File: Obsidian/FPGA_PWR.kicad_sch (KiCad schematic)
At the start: 52 parts, among them U1 XC7A35T-CSG325

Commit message: update with available components on LCSC
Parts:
- C100, C101, C102, C112, C121, C97, C98, C99: LCSC (none) -> C565524
- C103, C104, C105, C106, C107, C108, C117, C118, C156, C161, C162, C167, C168: LCSC (none) -> C318563
- C109, C110, C111, C119, C122: LCSC (none) -> C141660
- C113, C114, C115, C116, C120, C155, C89, C90, C91, C92, C93, C94, C95, C96: LCSC (none) -> C85926
- C157, C158, C159, C160, C163, C164, C165, C166, C169: LCSC (none) -> C190187
- L16: LCSC (none) -> C88966
- R114: LCSC (none) -> C413063
- U1: FT Rotation Offset (none) -> 0; LCSC (none) -> C1521749

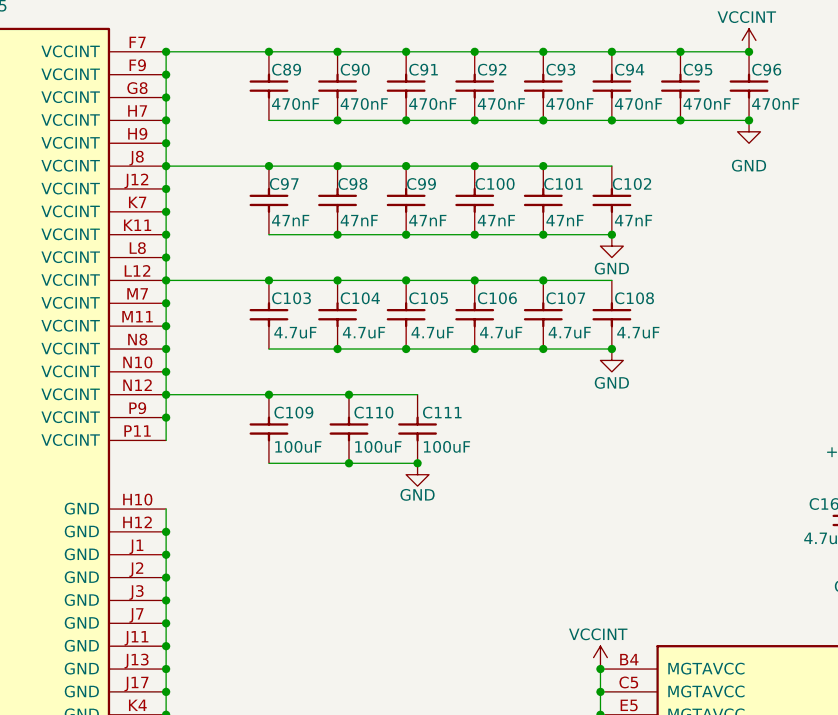
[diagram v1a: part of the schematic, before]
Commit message: Adding symbol library
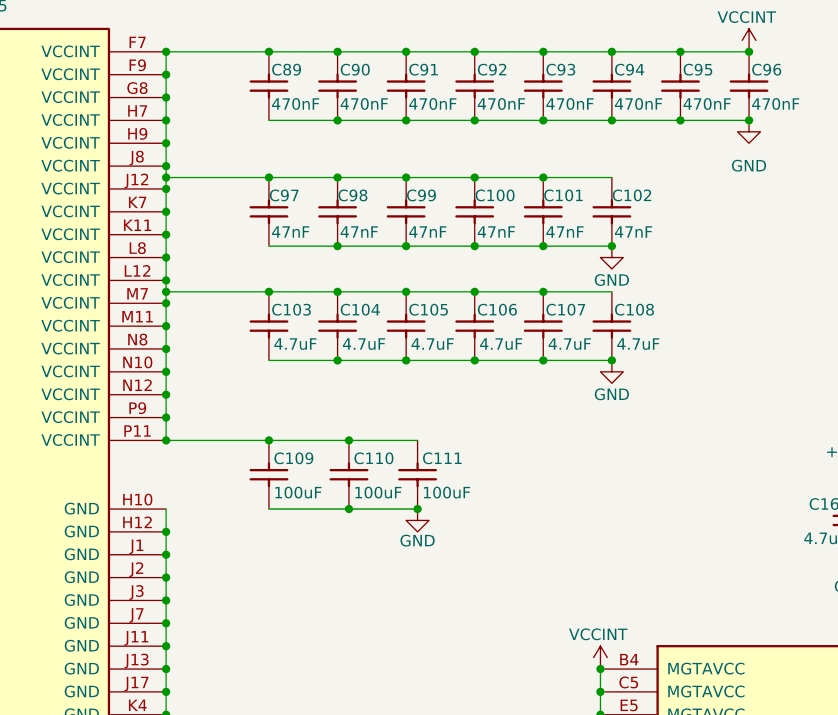
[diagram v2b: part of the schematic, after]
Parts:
- C100, C101, C102, C112, C121, C97, C98, C99: symbol Capacitors SMD:CC0201_47NF_6.3V_10%_X5R -> Library_Symbol:CC0201_47NF_6.3V_10%_X5R
- C103, C104, C105, C106, C107, C108, C117, C118, C156, C161, C162, C167, C168: symbol Capacitors SMD:CC0402_4.7UF_16V_20%_X5R -> Library_Symbol:CC0402_4.7UF_16V_20%_X5R
- C109, C110, C111, C119, C122: symbol Capacitors SMD:CC0805_100UF_6.3V_20%_X5R -> Library_Symbol:CC0805_100UF_6.3V_20%_X5R
- C113, C114, C115, C116, C120, C155, C89, C90, C91, C92, C93, C94, C95, C96: symbol Capacitors SMD:CC0201_470NF_4V_20%_X5R -> Library_Symbol:CC0201_470NF_4V_20%_X5R
- C157, C158, C159, C160, C163, C164, C165, C166, C169: symbol Capacitors SMD:CC0201_100NF_6.3V_10%_X5R -> Library_Symbol:CC0201_100NF_6.3V_10%_X5R
- L16: symbol Inductors SMD:IND0402_MURATA_BLM15HB221SN1 -> Library_Symbol:IND0402_MURATA_BLM15HB221SN1
- R114: symbol Resistors_SMD:R0402_100R_1%_0.1W_100PPM -> Library_Symbol:R0402_100R_1%_0.1W_100PPM
- U1: symbol FPGA_Xilinx_Artix7:XC7A35T-CSG325 -> Library_Symbol:XC7A35T-CSG325
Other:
- moved on the sheet: C100, C101, C102, C103, C104, C105, C106, C107, C108, C109, C110, C111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

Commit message: Correct Schematic errors
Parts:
- C100, C101, C102, C112, C113, C114, C115, C116, C120, C121, C155, C157, C158, C159, C160, C163, C164, C165, C166, C169, C89, C90, C91, C92, C93, C94, C95, C96, C97, C98, C99: footprint Capacitors SMD:CAPC0603X33N -> Footprint:CAPC0603X33N
- C103, C104, C105, C106, C107, C108, C117, C118, C156, C161, C162, C167, C168: footprint Capacitors SMD:CAPC1005X55N -> Footprint:CAPC1005X55N
- C109, C110, C111, C119, C122: footprint Capacitors SMD:CAPC2012X145N -> Footprint:CAPC2012X145N
- L16: footprint Inductors SMD:INDC1005X55N -> Footprint:INDC1005X55N
- R114: footprint RESC1005X40N -> Footprint:RESC1005X40N; Database Table Name (none) -> Resistors; Footprint Library (none) -> Resistors SMD; HelpURL (none) -> \\cern.ch\dfs\Applications\Altium\Datasheets\R0402_Phycomp_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
- U1: footprint Package_BGA:Xilinx_CSG325 -> Footprint:Xilinx_CSG325
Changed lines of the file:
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@@
 			)
 		)
-		(property "Footprint" "Capacitors SMD:CAPC1005X55N"
+		(property "Footprint" "Footprint:CAPC1005X55N"
 			(at 154.178 66.04 0)
 			(effects
@@
 			)
 		)
-		(property "Footprint" "Capacitors SMD:CAPC1005X55N"
+		(property "Footprint" "Footprint:CAPC1005X55N"
 			(at 146.558 66.04 0)
 			(effects
@@
 			)
 		)
-		(property "Footprint" "Capacitors SMD:CAPC2012X145N"
+		(property "Footprint" "Footprint:CAPC2012X145N"
 			(at 163.068 82.55 0)
 			(effects
@@
 			)
 		)
-		(property "Footprint" "Package_BGA:Xilinx_CSG325"
+		(property "Footprint" "Footprint:Xilinx_CSG325"
 			(at 213.36 107.95 0)
 			(effects
@@
 			)
 		)
-		(property "Footprint" "Capacitors SMD:CAPC0603X33N"
+		(property "Footprint" "Footprint:CAPC0603X33N"
 			(at 199.898 39.37 0)
 			(effects
@@
 			)
 		)
-		(property "Footprint" "Capacitors SMD:CAPC0603X33N"
+		(property "Footprint" "Footprint:CAPC0603X33N"
 			(at 154.178 39.37 0)
 			(effects
@@
 			)
 		)
-		(property "Footprint" "Capacitors SMD:CAPC1005X55N"
+		(property "Footprint" "Footprint:CAPC1005X55N"
 			(at 218.948 132.08 0)
 			(effects
@@
 			)
 		)
-		(property "Footprint" "Capacitors SMD:CAPC0603X33N"
+		(property "Footprint" "Footprint:CAPC0603X33N"
 			(at 161.798 53.34 0)
 			(effects
@@
 			)
 		)
-		(property "Footprint" "Capacitors SMD:CAPC0603X33N"
+		(property "Footprint" "Footprint:CAPC0603X33N"
 			(at 169.418 53.34 0)
 			(effects
@@
 			)
 		)
-		(property "Footprint" "Capacitors SMD:CAPC0603X33N"
+		(property "Footprint" "Footprint:CAPC0603X33N"
 			(at 198.628 132.08 0)
 			(effects
@@
 			)
 		)
-		(property "Footprint" "Capacitors SMD:CAPC0603X33N"
+		(property "Footprint" "Footprint:CAPC0603X33N"
 			(at 177.038 53.34 0)
 			(effects
@@
 			)
 		)
-		(property "Footprint" "Capacitors SMD:CAPC0603X33N"
+		(property "Footprint" "Footprint:CAPC0603X33N"
 			(at 184.658 39.37 0)
 			(effects
@@
 			)
 		)
-		(property "Footprint" "Capacitors SMD:CAPC0603X33N"
+		(property "Footprint" "Footprint:CAPC0603X33N"
 			(at 231.648 87.63 0)
 			(effects
@@
 			)
 		)
-		(property "Footprint" "Capacitors SMD:CAPC1005X55N"
+		(property "Footprint" "Footprint:CAPC1005X55N"
 			(at 177.038 66.04 0)
 			(effects
@@
 			)
 		)
-		(property "Footprint" "Capacitors SMD:CAPC0603X33N"
+		(property "Footprint" "Footprint:CAPC0603X33N"
 			(at 169.418 39.37 0)
 			(effects
@@
 			)
 		)
-		(property "Footprint" "Capacitors SMD:CAPC0603X33N"
+		(property "Footprint" "Footprint:CAPC0603X33N"
 			(at 70.358 33.02 0)
 			(effects
@@
 			)
 		)
-		(property "Footprint" "Capacitors SMD:CAPC0603X33N"
+		(property "Footprint" "Footprint:CAPC0603X33N"
 			(at 146.558 53.34 0)
 			(effects
@@
 			)
 		)
-		(property "Footprint" "Capacitors SMD:CAPC2012X145N"
+		(property "Footprint" "Footprint:CAPC2012X145N"
 			(at 146.558 82.55 0)
 			(effects
@@
 			)
 		)
-		(property "Footprint" "Capacitors SMD:CAPC0603X33N"
+		(property "Footprint" "Footprint:CAPC0603X33N"
 			(at 65.278 74.93 0)
 			(effects
@@
 			)
 		)
-		(property "Footprint" "Capacitors SMD:CAPC0603X33N"
+		(property "Footprint" "Footprint:CAPC0603X33N"
 			(at 224.028 87.63 0)
 			(effects
@@
 			)
 		)
-		(property "Footprint" "Capacitors SMD:CAPC0603X33N"
+		(property "Footprint" "Footprint:CAPC0603X33N"
 			(at 61.468 57.15 0)
 			(effects
@@
 			)
 		)
-		(property "Footprint" "Capacitors SMD:CAPC0603X33N"
+		(property "Footprint" "Footprint:CAPC0603X33N"
 			(at 79.248 33.02 0)
 			(effects
@@
 			)
 		)
-		(property "Footprint" "Capacitors SMD:CAPC2012X145N"
+		(property "Footprint" "Footprint:CAPC2012X145N"
 			(at 155.448 82.55 0)
 			(effects
@@
 			)
 		)
-		(property "Footprint" "Capacitors SMD:CAPC0603X33N"
+		(property "Footprint" "Footprint:CAPC0603X33N"
 			(at 254.508 87.63 0)
 			(effects
@@
 			)
 		)
-		(property "Footprint" "Capacitors SMD:CAPC2012X145N"
+		(property "Footprint" "Footprint:CAPC2012X145N"
 			(at 24.638 33.02 0)
 			(effects
@@
 			)
 		)
-		(property "Footprint" "Package_BGA:Xilinx_CSG325"
+		(property "Footprint" "Footprint:Xilinx_CSG325"
 			(at 101.6 102.87 0)
 			(effects
@@
 			)
 		)
-		(property "Footprint" "Capacitors SMD:CAPC0603X33N"
+		(property "Footprint" "Footprint:CAPC0603X33N"
 			(at 62.738 33.02 0)
 			(effects
@@
 			)
 		)
-		(property "Footprint" "RESC1005X40N"
+		(property "Footprint" "Footprint:RESC1005X40N"
 			(at 251.46 141.478 0)
 			(effects
@@
 			)
 		)
+		(property "Database Table Name" "Resistors"
+			(at 251.46 115.57 0)
+			(effects
+				(font
+					(size 1.27 1.27)
+				)
+				(hide yes)
+			)
+		)
+		(property "Footprint Library" "Resistors SMD"
+			(at 251.46 115.57 0)
+			(effects
+				(font
+					(size 1.27 1.27)
+				)
+				(hide yes)
+			)
+		)
+		(property "HelpURL" "\\\\cern.ch\\dfs\\Applications\\Altium\\Datasheets\\R0402_Phycomp_RC0402.pdf"
+			(at 251.46 115.57 0)
+			(effects
+				(font
+					(size 1.27 1.27)
+				)
+				(hide yes)
+			)
+		)
 		(pin "1"
 		)
@@
 			)
 		)
-		(property "Footprint" "Capacitors SMD:CAPC0603X33N"
+		(property "Footprint" "Footprint:CAPC0603X33N"
 			(at 177.038 39.37 0)
 			(effects
@@
 			)
 		)
-		(property "Footprint" "Capacitors SMD:CAPC0603X33N"
+		(property "Footprint" "Footprint:CAPC0603X33N"
 			(at 74.168 74.93 0)
 			(effects
@@
 			)
 		)
-		(property "Footprint" "Capacitors SMD:CAPC1005X55N"
+		(property "Footprint" "Footprint:CAPC1005X55N"
 			(at 33.528 33.02 0)
 			(effects
@@
 			)
 		)
-		(property "Footprint" "Capacitors SMD:CAPC2012X145N"
+		(property "Footprint" "Footprint:CAPC2012X145N"
 			(at 57.658 74.93 0)
 			(effects
@@
 			)
 		)
-		(property "Footprint" "Inductors SMD:INDC1005X55N"
+		(property "Footprint" "Footprint:INDC1005X55N"
 			(at 39.37 56.388 0)
 			(effects
@@
 			)
 		)
-		(property "Footprint" "Capacitors SMD:CAPC0603X33N"
+		(property "Footprint" "Footprint:CAPC0603X33N"
 			(at 183.388 132.08 0)
 			(effects
@@
 			)
 		)
-		(property "Footprint" "Capacitors SMD:CAPC0603X33N"
+		(property "Footprint" "Footprint:CAPC0603X33N"
 			(at 184.658 53.34 0)
 			(effects
@@
 			)
 		)
-		(property "Footprint" "Capacitors SMD:CAPC0603X33N"
+		(property "Footprint" "Footprint:CAPC0603X33N"
 			(at 55.118 33.02 0)
 			(effects
@@
 			)
 		)
-		(property "Footprint" "Capacitors SMD:CAPC1005X55N"
+		(property "Footprint" "Footprint:CAPC1005X55N"
 			(at 211.328 132.08 0)
 			(effects
@@
 			)
 		)
-		(property "Footprint" "Capacitors SMD:CAPC0603X33N"
+		(property "Footprint" "Footprint:CAPC0603X33N"
 			(at 192.278 39.37 0)
 			(effects
@@
 			)
 		)
-		(property "Footprint" "Capacitors SMD:CAPC0603X33N"
+		(property "Footprint" "Footprint:CAPC0603X33N"
 			(at 246.888 87.63 0)
 			(effects
@@
 			)
 		)
-		(property "Footprint" "Capacitors SMD:CAPC1005X55N"
+		(property "Footprint" "Footprint:CAPC1005X55N"
 			(at 169.418 66.04 0)
 			(effects
@@
 			)
 		)
-		(property "Footprint" "Capacitors SMD:CAPC1005X55N"
+		(property "Footprint" "Footprint:CAPC1005X55N"
 			(at 161.798 66.04 0)
 			(effects
@@
 			)
 		)
-		(property "Footprint" "Capacitors SMD:CAPC0603X33N"
+		(property "Footprint" "Footprint:CAPC0603X33N"
 			(at 191.008 132.08 0)
 			(effects
@@
 			)
 		)
-		(property "Footprint" "Capacitors SMD:CAPC0603X33N"
+		(property "Footprint" "Footprint:CAPC0603X33N"
 			(at 154.178 53.34 0)
 			(effects
@@
 			)
 		)
-		(property "Footprint" "Capacitors SMD:CAPC0603X33N"
+		(property "Footprint" "Footprint:CAPC0603X33N"
 			(at 146.558 39.37 0)
 			(effects
@@
 			)
 		)
-		(property "Footprint" "Capacitors SMD:CAPC1005X55N"
+		(property "Footprint" "Footprint:CAPC1005X55N"
 			(at 202.692 87.63 0)
 			(effects
@@
 			)
 		)
-		(property "Footprint" "Capacitors SMD:CAPC1005X55N"
+		(property "Footprint" "Footprint:CAPC1005X55N"
 			(at 195.072 87.63 0)
 			(effects
@@
 			)
 		)
-		(property "Footprint" "Capacitors SMD:CAPC0603X33N"
+		(property "Footprint" "Footprint:CAPC0603X33N"
 			(at 239.268 87.63 0)
 			(effects
@@
 			)
 		)
-		(property "Footprint" "Capacitors SMD:CAPC1005X55N"
+		(property "Footprint" "Footprint:CAPC1005X55N"
 			(at 38.608 57.15 0)
 			(effects
@@
 			)
 		)
-		(property "Footprint" "Capacitors SMD:CAPC1005X55N"
+		(property "Footprint" "Footprint:CAPC1005X55N"
 			(at 41.148 33.02 0)
 			(effects
@@
 			)
 		)
-		(property "Footprint" "Capacitors SMD:CAPC1005X55N"
+		(property "Footprint" "Footprint:CAPC1005X55N"
 			(at 184.658 66.04 0)
 			(effects
@@
 			)
 		)
-		(property "Footprint" "Capacitors SMD:CAPC0603X33N"
+		(property "Footprint" "Footprint:CAPC0603X33N"
 			(at 47.498 33.02 0)
 			(effects
@@
 			)
 		)
-		(property "Footprint" "Capacitors SMD:CAPC0603X33N"
+		(property "Footprint" "Footprint:CAPC0603X33N"
 			(at 204.978 132.08 0)
 			(effects
@@
 			)
 		)
-		(property "Footprint" "Capacitors SMD:CAPC0603X33N"
+		(property "Footprint" "Footprint:CAPC0603X33N"
 			(at 161.798 39.37 0)
 			(effects

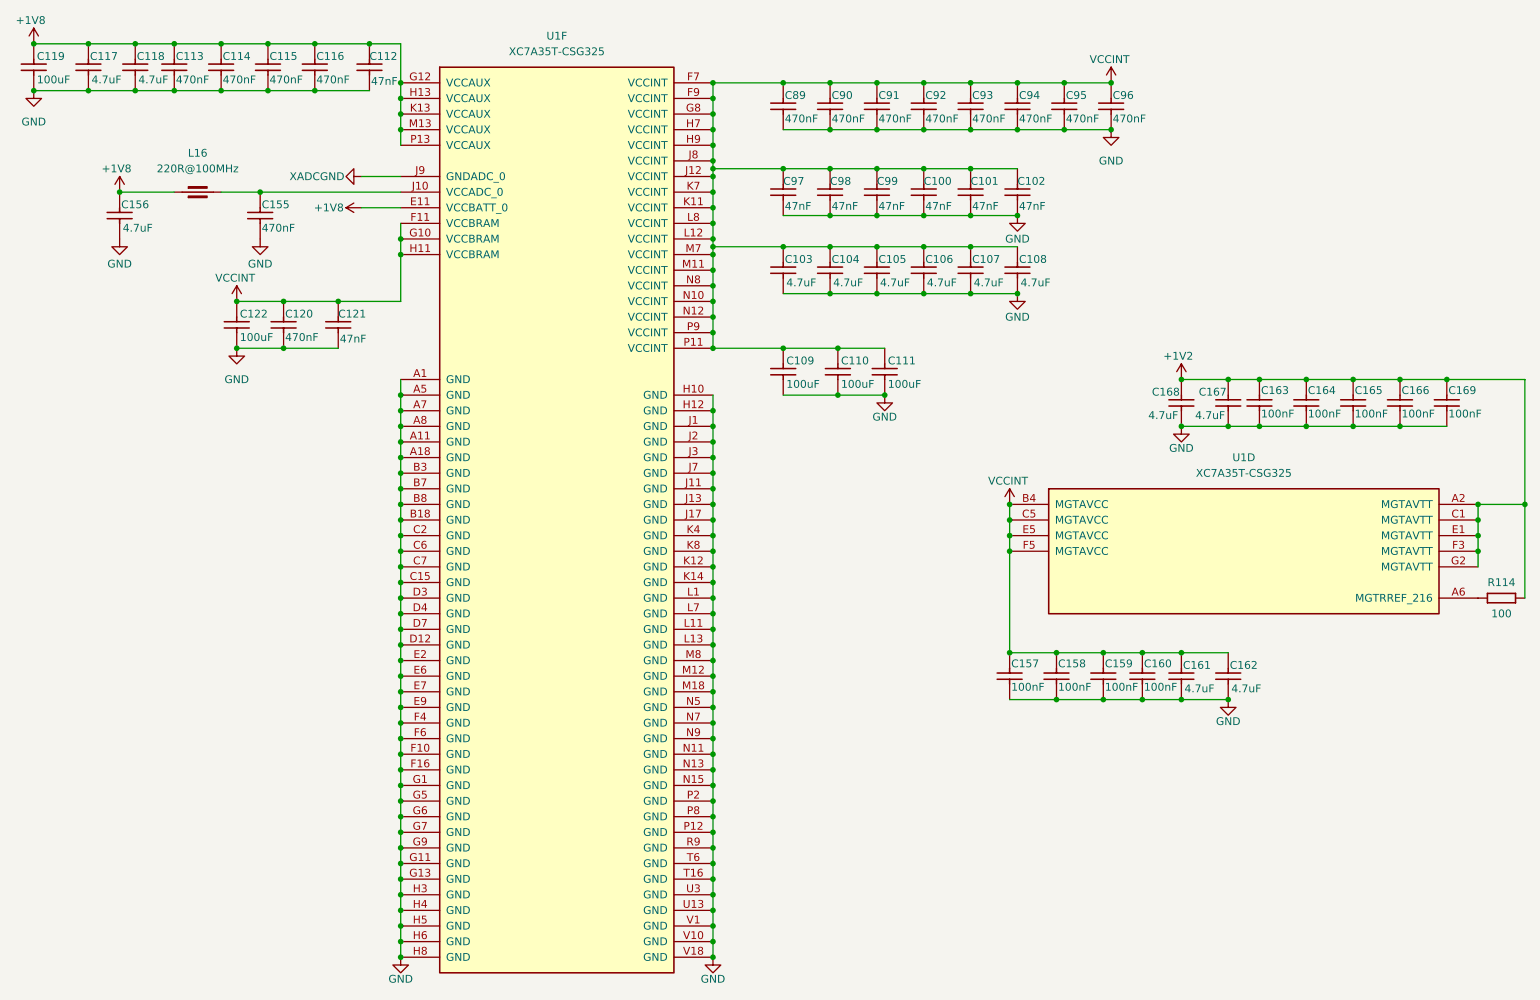
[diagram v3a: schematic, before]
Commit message: deleting two labels on 1V net, replacing with VCCINT_1V
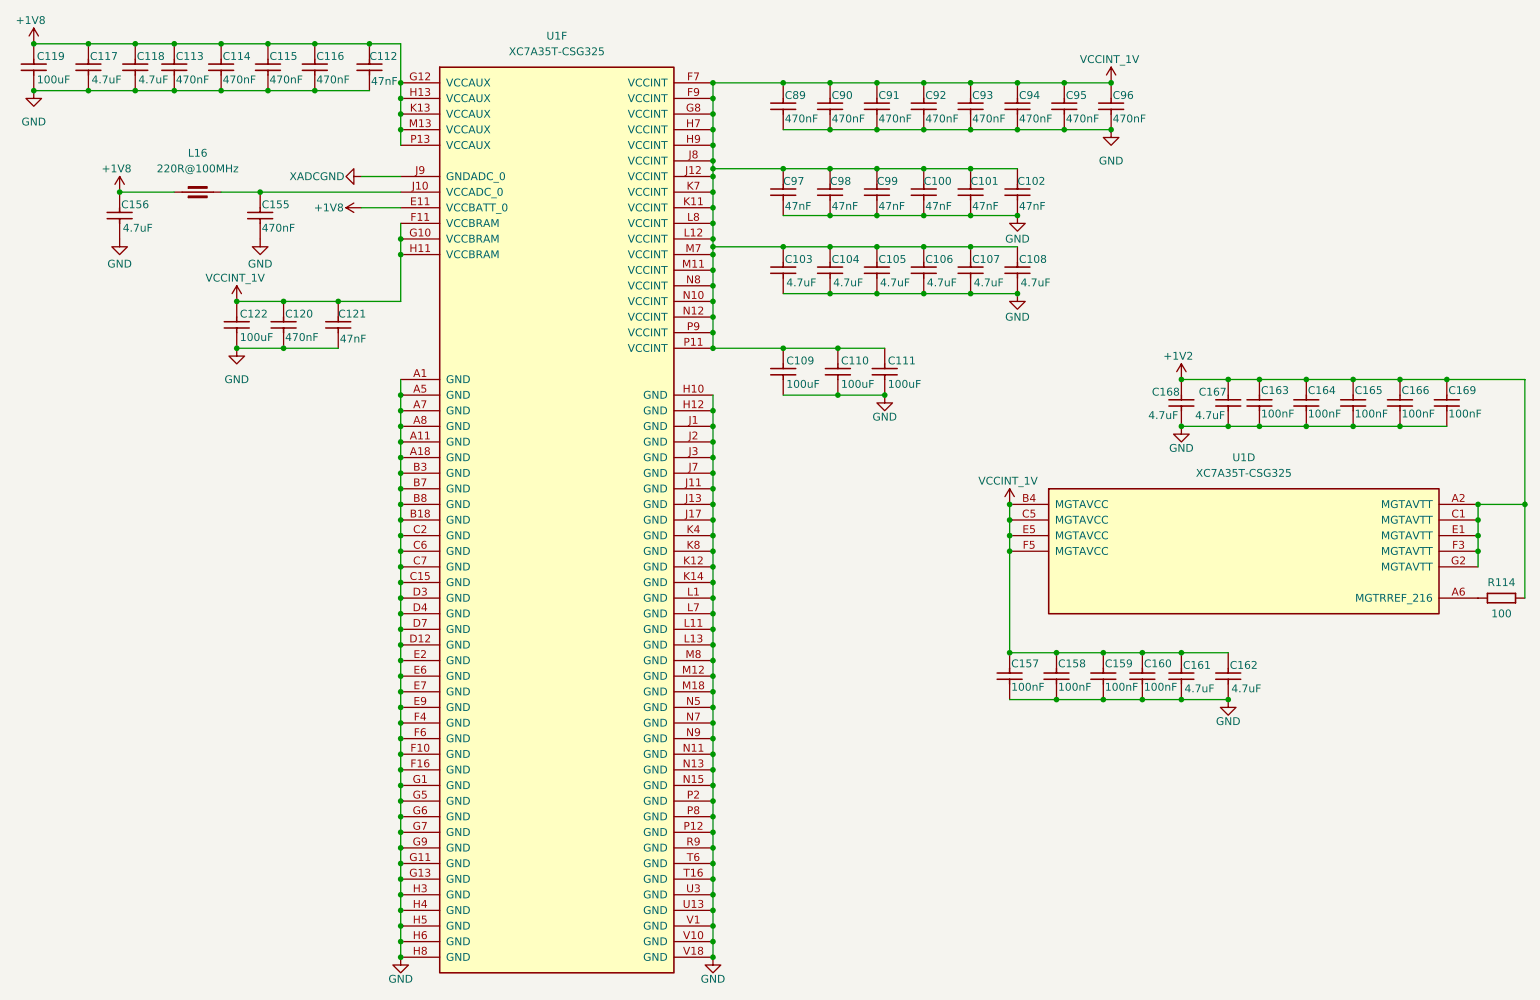
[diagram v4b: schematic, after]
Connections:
- net VCCINT renamed VCCINT_1V
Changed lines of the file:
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@@
 			)
 		)
-		(property "Value" "VCCINT"
+		(property "Value" "VCCINT_1V"
 			(at 175.006 96.52 0)
 			(effects
@@
 			)
 		)
-		(property "Value" "VCCINT"
+		(property "Value" "VCCINT_1V"
 			(at 191.516 27.94 0)
 			(effects
@@
 			)
 		)
-		(property "Value" "VCCINT"
+		(property "Value" "VCCINT_1V"
 			(at 49.276 63.5 0)
 			(effects
